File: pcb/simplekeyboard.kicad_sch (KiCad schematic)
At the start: 34 parts, among them J1 USB_C_Receptacle_USB2.0_16P, J2 Conn_ARM_JTAG_SWD_10, SW62 SW_SPDT, SW63 SW_Push, U1 STM32F072CBT6, U2 USBLC6-2SC6, U3 LD39050PU33R, U4 MCP23017_SO, U5 MCP23008-xSO

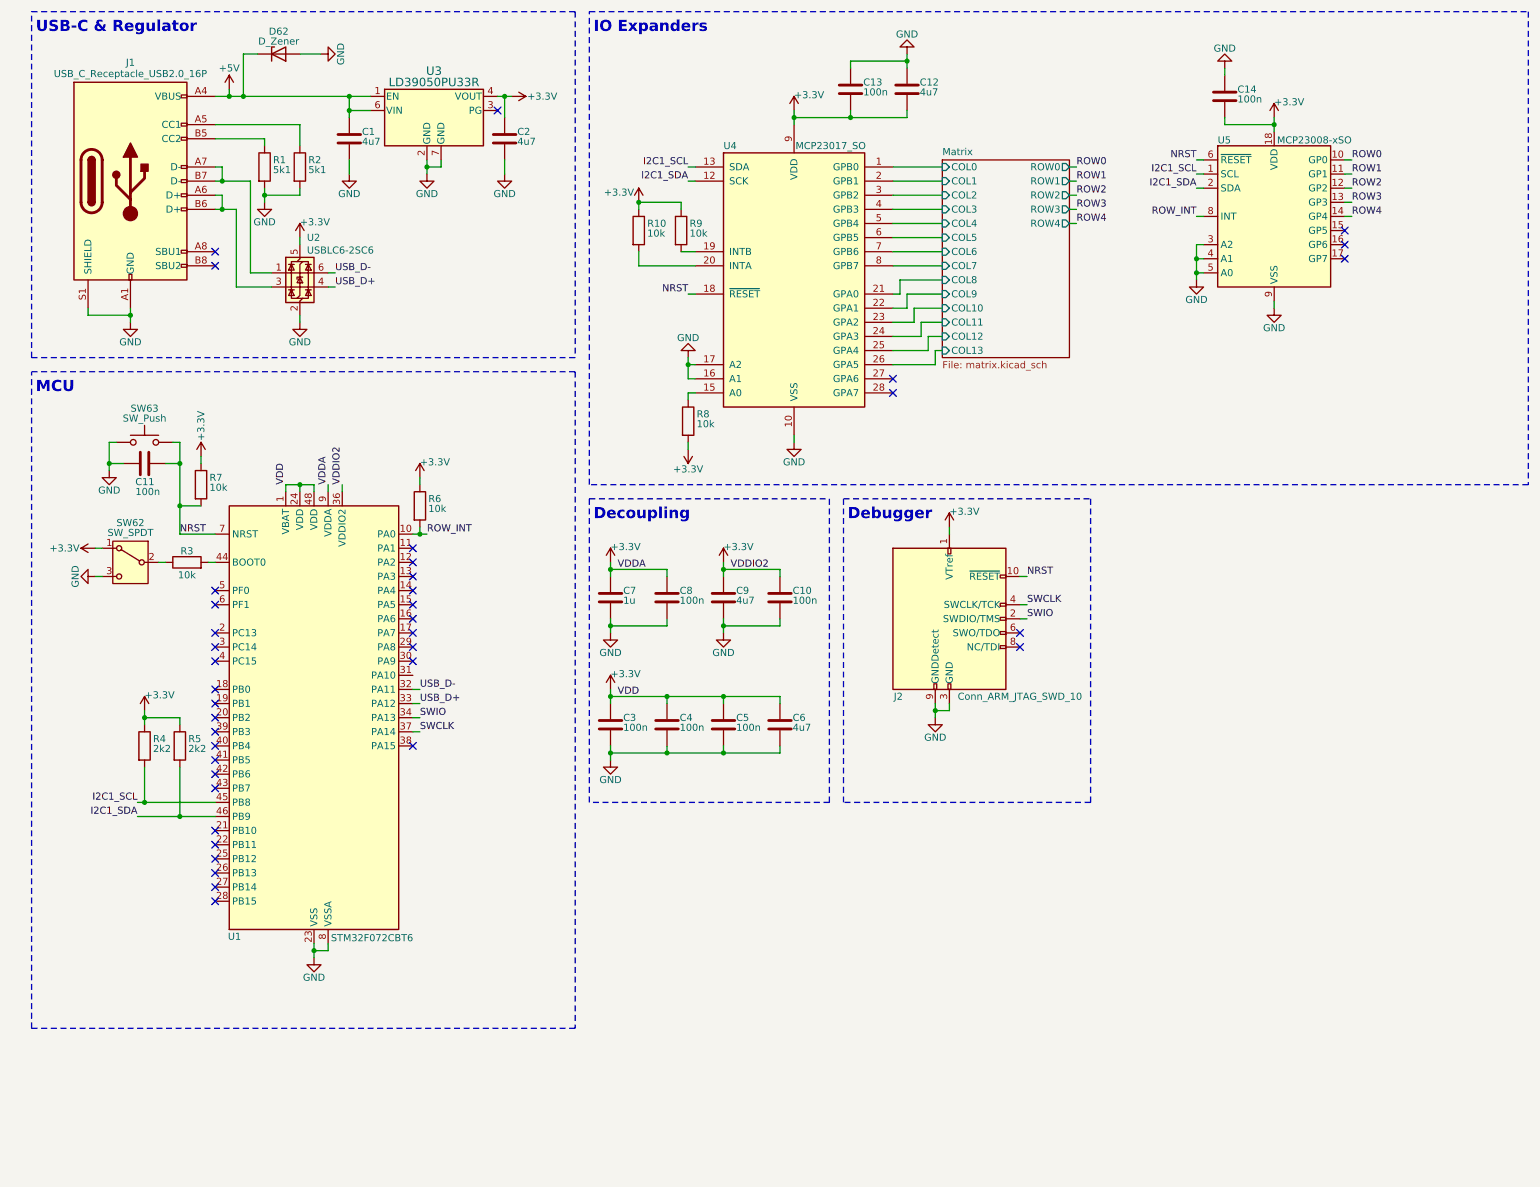
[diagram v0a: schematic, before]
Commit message: Clear board and add mounting holes
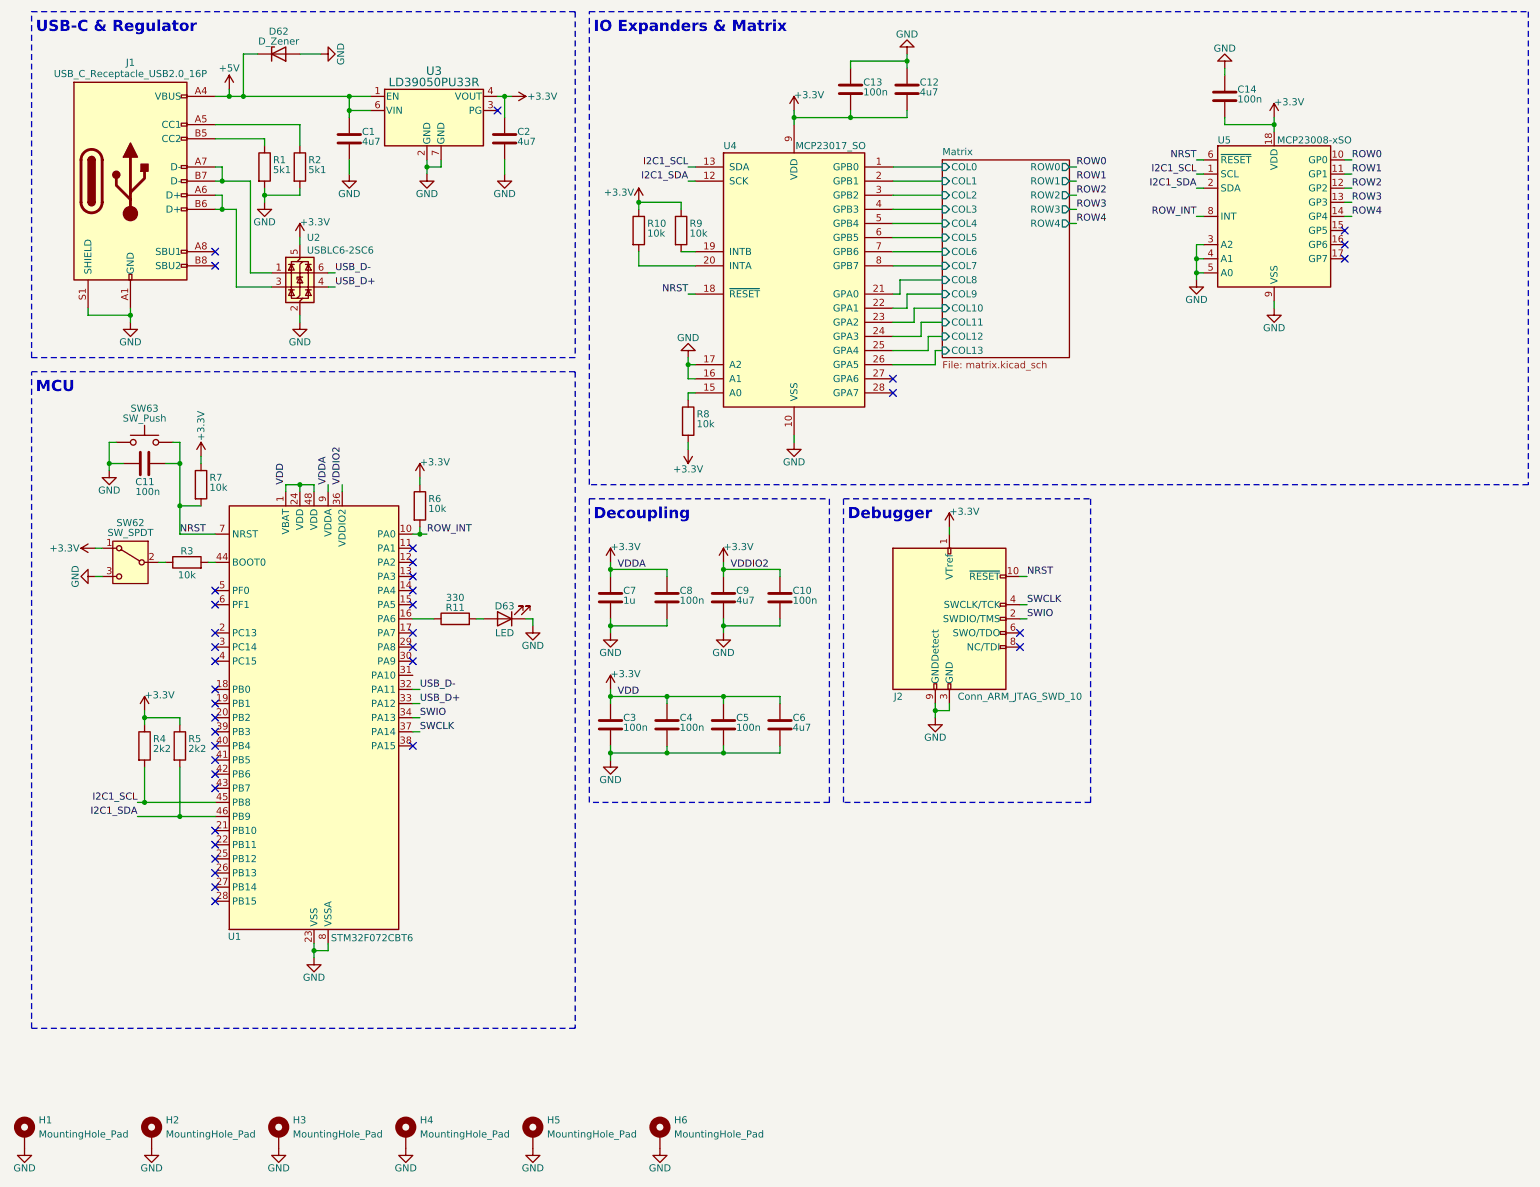
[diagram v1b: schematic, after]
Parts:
- added D63: LED, LED_SMD:LED_0201_0603Metric, symbol Device:LED
- added H1: MountingHole_Pad, Keyboard_Mounts:2.5mm, symbol Mechanical:MountingHole_Pad
- added H2, H3, H4: MountingHole_Pad, Keyboard_Mounts:2.5mm_Oblong, symbol Mechanical:MountingHole_Pad
- added H5, H6: MountingHole_Pad, Keyboard_Mounts:2.5mm_Wide, symbol Mechanical:MountingHole_Pad
- added R11: 330, Resistor_SMD:R_0603_1608Metric, symbol Device:R
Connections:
- net GND: now also D63.1 (K), H1.1, H2.1, H3.1, H4.1, H5.1, H6.1
- net at U1.16 (PA6): now also R11.1
- new net: D63.2 (A), R11.2
- no-connect marks 39 -> 38
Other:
- note added: "IO Expanders & Matrix"
- note removed: "IO Expanders"

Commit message: Routing almost complete
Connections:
- net USB_D+: now also J1.A6 (D+), J1.B6 (D+), U2.3 (I/O2)
- net USBC_D-: now reaches J1.A7 (D-), J1.B7 (D-), U2.1 (I/O1)
- no-connect marks 38 -> 39
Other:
- moved on the sheet: U2
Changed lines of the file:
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@@
 	)
 	(no_connect
+		(at 82.55 133.35)
+	)
+	(no_connect
 		(at 82.55 118.11)
 	)
@@
 	(wire
 		(pts
-			(xy 62.23 54.61) (xy 62.23 55.88)
+			(xy 68.58 54.61) (xy 68.58 55.88)
 		)
 		(stroke
@@
 	(wire
 		(pts
-			(xy 67.31 60.96) (xy 68.58 60.96)
+			(xy 73.66 60.96) (xy 74.93 60.96)
 		)
 		(stroke
@@
 	(wire
 		(pts
-			(xy 57.15 63.5) (xy 50.8 63.5)
+			(xy 63.5 63.5) (xy 50.8 63.5)
 		)
 		(stroke
@@
 	(wire
 		(pts
-			(xy 67.31 63.5) (xy 68.58 63.5)
+			(xy 73.66 63.5) (xy 74.93 63.5)
 		)
 		(stroke
@@
 	(wire
 		(pts
-			(xy 57.15 60.96) (xy 53.34 60.96)
+			(xy 63.5 60.96) (xy 53.34 60.96)
 		)
 		(stroke
@@
 	(wire
 		(pts
-			(xy 62.23 69.85) (xy 62.23 68.58)
+			(xy 68.58 69.85) (xy 68.58 68.58)
 		)
 		(stroke
@@
 		)
 	)
+	(label "USB_D+"
+		(at 50.8 63.5 0)
+		(effects
+			(font
+				(size 1.27 1.27)
+			)
+			(justify left bottom)
+		)
+	)
 	(label "NRST"
 		(at 40.64 107.95 0)
@@
 		)
 	)
+	(label "USBC_D-"
+		(at 53.34 60.96 0)
+		(effects
+			(font
+				(size 1.27 1.27)
+			)
+			(justify left bottom)
+		)
+	)
 	(label "VDDIO2"
 		(at 139.7 114.3 0)
@@
 	)
 	(label "USB_D+"
-		(at 68.58 63.5 0)
+		(at 74.93 63.5 0)
 		(effects
 			(font
@@
 	)
 	(label "USB_D-"
-		(at 68.58 60.96 0)
+		(at 74.93 60.96 0)
 		(effects
 			(font
@@
 	(symbol
 		(lib_id "power:GND")
-		(at 62.23 69.85 0)
+		(at 68.58 69.85 0)
 		(unit 1)
 		(exclude_from_sim no)
@@
 		(dnp no)
 		(property "Reference" "#PWR09"
-			(at 62.23 76.2 0)
+			(at 68.58 76.2 0)
 			(effects
 				(font
@@
 		)
 		(property "Value" "GND"
-			(at 62.23 73.406 0)
+			(at 68.58 73.406 0)
 			(effects
 				(font
@@
 		)
 		(property "Footprint" ""
-			(at 62.23 69.85 0)
+			(at 68.58 69.85 0)
 			(effects
 				(font
@@
 		)
 		(property "Datasheet" ""
-			(at 62.23 69.85 0)
+			(at 68.58 69.85 0)
 			(effects
 				(font
@@
 		)
 		(property "Description" "Power symbol creates a global label with name \"GND\" , ground"
-			(at 62.23 69.85 0)
+			(at 68.58 69.85 0)
 			(effects
 				(font
@@
 	(symbol
 		(lib_id "Power_Protection:USBLC6-2SC6")
-		(at 62.23 60.96 0)
+		(at 68.58 60.96 0)
 		(unit 1)
 		(exclude_from_sim no)
@@
 		(dnp no)
 		(property "Reference" "U2"
-			(at 63.5 54.61 0)
+			(at 69.85 54.61 0)
 			(effects
 				(font
@@
 		)
 		(property "Value" "USBLC6-2SC6"
-			(at 63.5 56.896 0)
+			(at 69.85 56.896 0)
 			(effects
 				(font
@@
 		)
 		(property "Footprint" "Package_TO_SOT_SMD:SOT-23-6"
-			(at 63.5 67.31 0)
+			(at 69.85 67.31 0)
 			(effects
 				(font
@@
 		)
 		(property "Datasheet" "https://www.st.com/resource/en/datasheet/usblc6-2.pdf"
-			(at 63.5 69.215 0)
+			(at 69.85 69.215 0)
 			(effects
 				(font
@@
 		)
 		(property "Description" "Very low capacitance ESD protection diode, 2 data-line, SOT-23-6"
-			(at 62.23 60.96 0)
+			(at 68.58 60.96 0)
 			(effects
 				(font
@@
 	(symbol
 		(lib_id "power:+3.3V")
-		(at 62.23 54.61 0)
+		(at 68.58 54.61 0)
 		(unit 1)
 		(exclude_from_sim no)
@@
 		(dnp no)
 		(property "Reference" "#PWR035"
-			(at 62.23 58.42 0)
+			(at 68.58 58.42 0)
 			(effects
 				(font
@@
 		)
 		(property "Value" "+3.3V"
-			(at 62.23 51.816 0)
+			(at 68.58 51.816 0)
 			(effects
 				(font
@@
 		)
 		(property "Footprint" ""
-			(at 62.23 54.61 0)
+			(at 68.58 54.61 0)
 			(effects
 				(font
@@
 		)
 		(property "Datasheet" ""
-			(at 62.23 54.61 0)
+			(at 68.58 54.61 0)
 			(effects
 				(font
@@
 		)
 		(property "Description" "Power symbol creates a global label with name \"+3.3V\""
-			(at 62.23 54.61 0)
+			(at 68.58 54.61 0)
 			(effects
 				(font

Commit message: Finished routing and various fixes
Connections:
- net +3.3V: no longer U2.5 (VBUS)
- net +5V: now also U2.5 (VBUS)
- net USB_D+: no longer J1.A6 (D+), J1.B6 (D+), U2.3 (I/O2)
- new net USBC_D+: J1.A6 (D+), J1.B6 (D+), U2.3 (I/O2)
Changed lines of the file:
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@@
 		)
 	)
-	(label "USB_D+"
+	(label "USBC_D+"
 		(at 50.8 63.5 0)
 		(effects
@@
 			)
 		)
-		(property "Value" "+3.3V"
+		(property "Value" "+5V"
 			(at 68.58 51.816 0)
 			(effects
